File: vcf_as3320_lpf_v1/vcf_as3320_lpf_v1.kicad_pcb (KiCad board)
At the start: 2 copper layers, 15 x 100 mm, 87 parts, among them J1 Conn_02x05_Odd_Even, J4 IN1, J5 OUT_2, U1 LM358, U2 TL072, U3 AS3320, U4 LM79L05_TO92, U5 LM358

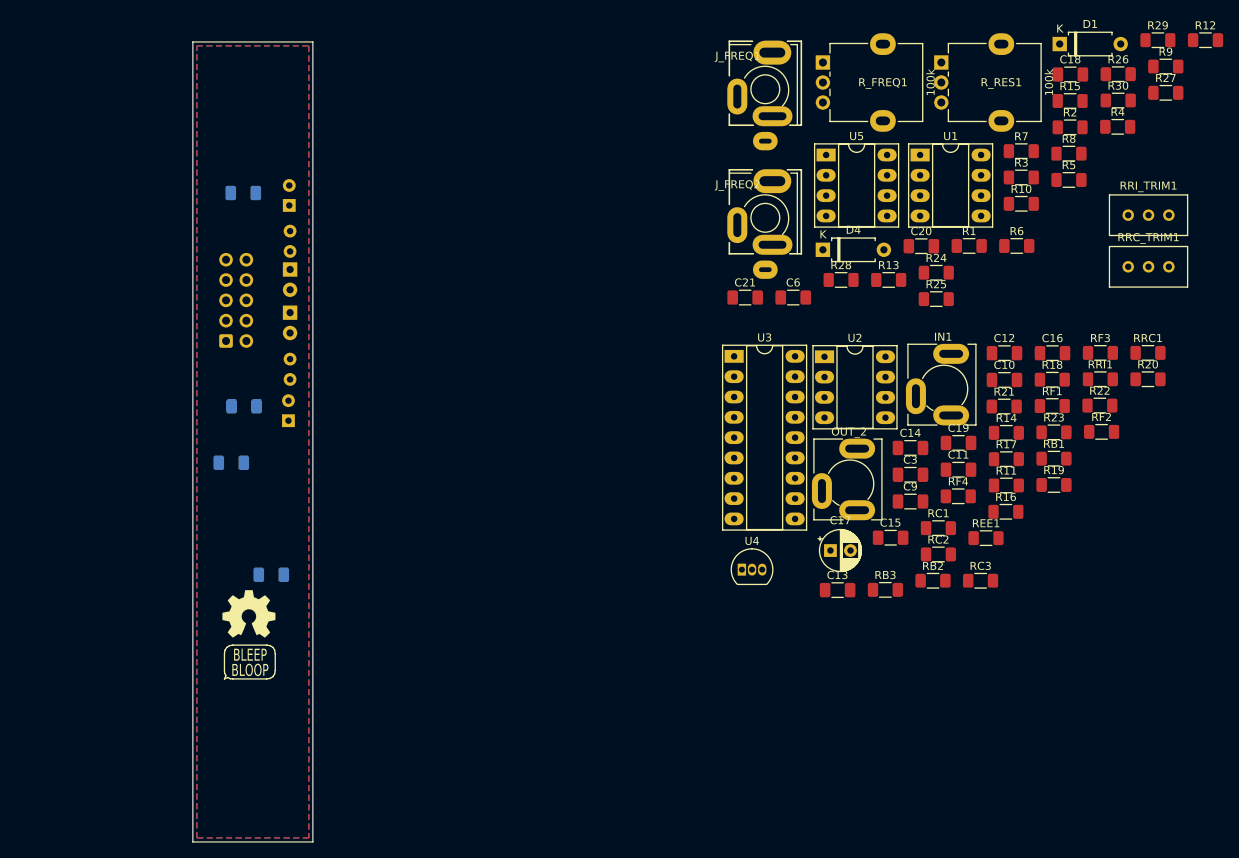
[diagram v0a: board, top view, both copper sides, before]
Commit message: Draft layout done no routing
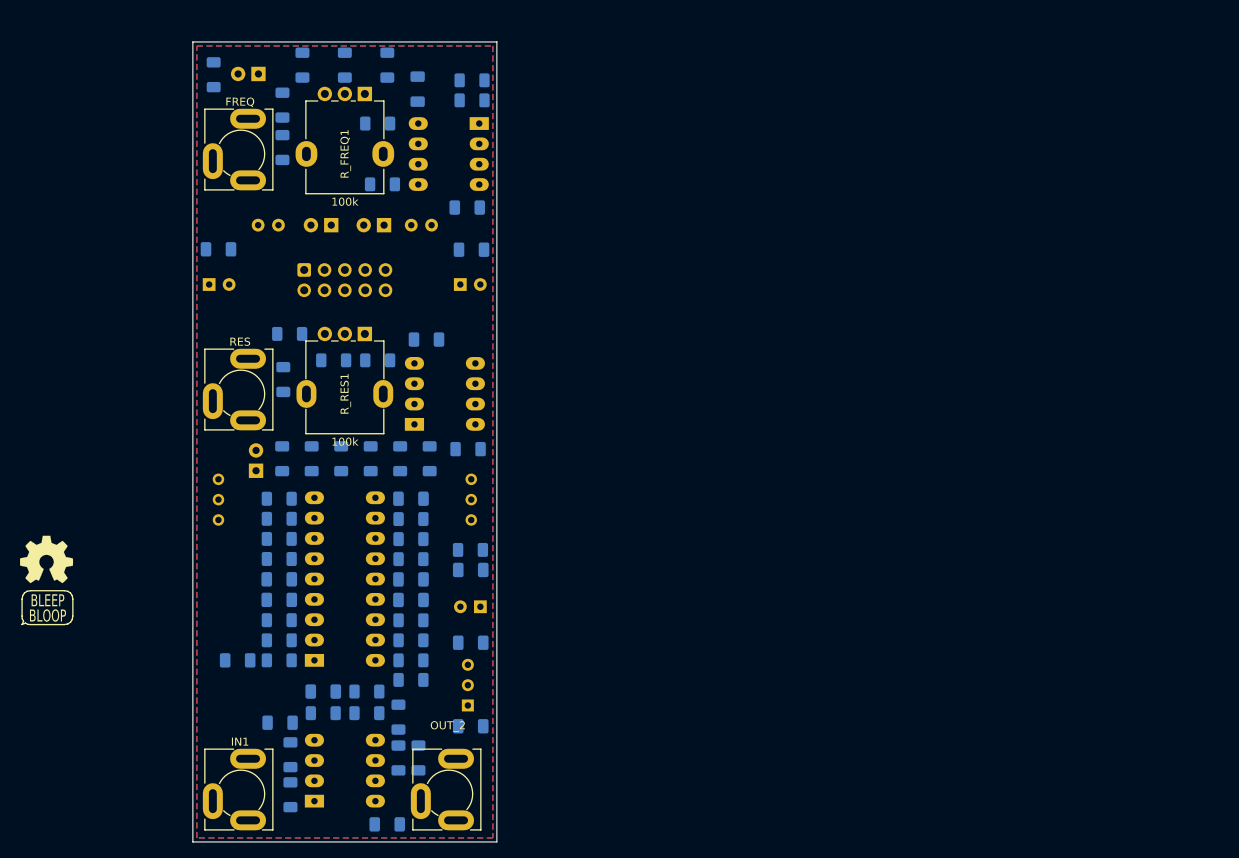
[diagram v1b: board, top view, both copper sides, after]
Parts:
- removed J_FREQ2: FREQ, My Stuff:Jack_3.5mm_MJ-355W_and_PJ398SM_Vertical
- added J_RES1: RES, My Stuff:Jack_3.5mm_MJ-355W_Vertical, F.Cu at (146.0, 94.0)
- C10, C11, C12, C13, C14, C15, C16, C17, C18, C19, C20, C21, C3, C6, C9, R1, R10, R11, R12, R13, R14, R15, R16, R17, R18, R19, R2, R20, R21, R22, R23, R24, R25, R26, R27, R28, R29, R3, R30, R4, R5, R6, R7, R8, R9, RB1, RB2, RB3, RC1, RC2, RC3, REE1, RF1, RF2, RF3, RF4, RRC1, RRC_TRIM1, RRI1, RRI_TRIM1, U1, U2, U3, U5: moved to B.Cu
- D1, D4: footprint Diode_THT:D_A-405_P7.62mm_Horizontal -> Diode_THT:D_A-405_P2.54mm_Vertical_KathodeUp; moved to B.Cu
- J_FREQ1: footprint My Stuff:Jack_3.5mm_MJ-355W_and_PJ398SM_Vertical -> My Stuff:Jack_3.5mm_MJ-355W_Vertical
- U4: footprint Package_TO_SOT_THT:TO-92_Inline -> Package_TO_SOT_THT:TO-92_Inline_Wide; moved to B.Cu
- moved RRI_TRIM1 124.8 mm to (143.2, 109.8), turned to -90 degrees
- moved R12 120.2 mm to (152.1, 86.5)
- moved R4 113.2 mm to (142.6, 54.1), turned to 90 degrees
- moved R30 110.3 mm to (154.9, 102.1), turned to -90 degrees
- moved R26 108.4 mm to (158.5, 102.1), turned to 90 degrees
- moved R27 106.1 mm to (165.9, 102.1), turned to 90 degrees
- moved RF3 105.8 mm to (150.8, 114.6)
- moved R29 105.0 mm to (169.6, 102.1), turned to 90 degrees
- moved RRI1 103.7 mm to (150.8, 107.1), turned to 180 degrees
- moved R22 103.6 mm to (150.8, 109.6)
- moved R20 102.8 mm to (165.7, 134.4), turned to 90 degrees
- moved J4 101.4 mm to (146.0, 144.0)
- moved D1 100.2 mm to (148.2, 54.0), turned to 180 degrees
- moved R9 99.0 mm to (163.7, 67.8)
- moved R2 98.5 mm to (151.2, 57.9), turned to -90 degrees
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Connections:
- R_FREQ1 pad 1: Net-(R2-Pad1) -> Net-(R1-Pad2)
- R_FREQ1 pad 3: Net-(R1-Pad2) -> Net-(R2-Pad1)
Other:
- board size 15 x 100 mm -> 38 x 100 mm
- board text added: "Make new fp for res pot for plastic trim pots"
- board text added: "feedback"
- board text added: "input"
- board text added: "output"

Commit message: Draft routing done
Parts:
- moved R12 13.9 mm to (166.0, 86.1), turned to 180 degrees
- moved R13 3.19 mm to (159.3, 92.5)
- moved LOGO3 2.84 mm to (121.2, 111.9)
- moved C21 2.31 mm to (171.4, 86.5)
- moved R7 0.70 mm to (174.2, 57.3)
- moved R8 0.70 mm to (174.2, 54.8)
- moved R15 0.70 mm to (162.4, 89.8)
- turned C20 to 180 degrees
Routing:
- net -12V: track 0.00 -> 188.2 mm, vias 0 -> 1
- net +12V: track 0.00 -> 157.1 mm, vias 0 -> 1
- net Net-(R17-Pad2): track 0.00 -> 67.2 mm
- net /CV Inputs/FREQ_CV: track 0.00 -> 63.4 mm, vias 0 -> 1
- net Net-(C3-Pad2): track 0.00 -> 30.9 mm
- net Net-(C19-Pad2): track 0.00 -> 30.2 mm
- net Net-(RC1-Pad2): track 0.00 -> 28.0 mm, vias 0 -> 1
- net Net-(RC2-Pad2): track 0.00 -> 26.5 mm, vias 0 -> 1
- net Net-(RRC1-Pad2): track 0.00 -> 25.5 mm
- net Net-(RC3-Pad2): track 0.00 -> 24.2 mm, vias 0 -> 1
- net Net-(R6-Pad1): track 0.00 -> 22.5 mm
- net Net-(J_FREQ1-PadT): track 0.00 -> 20.8 mm
- net /CV Inputs/RES_CV: track 0.00 -> 19.9 mm
- net Net-(R27-Pad1): track 0.00 -> 18.7 mm
- net -5V: track 0.00 -> 17.5 mm
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
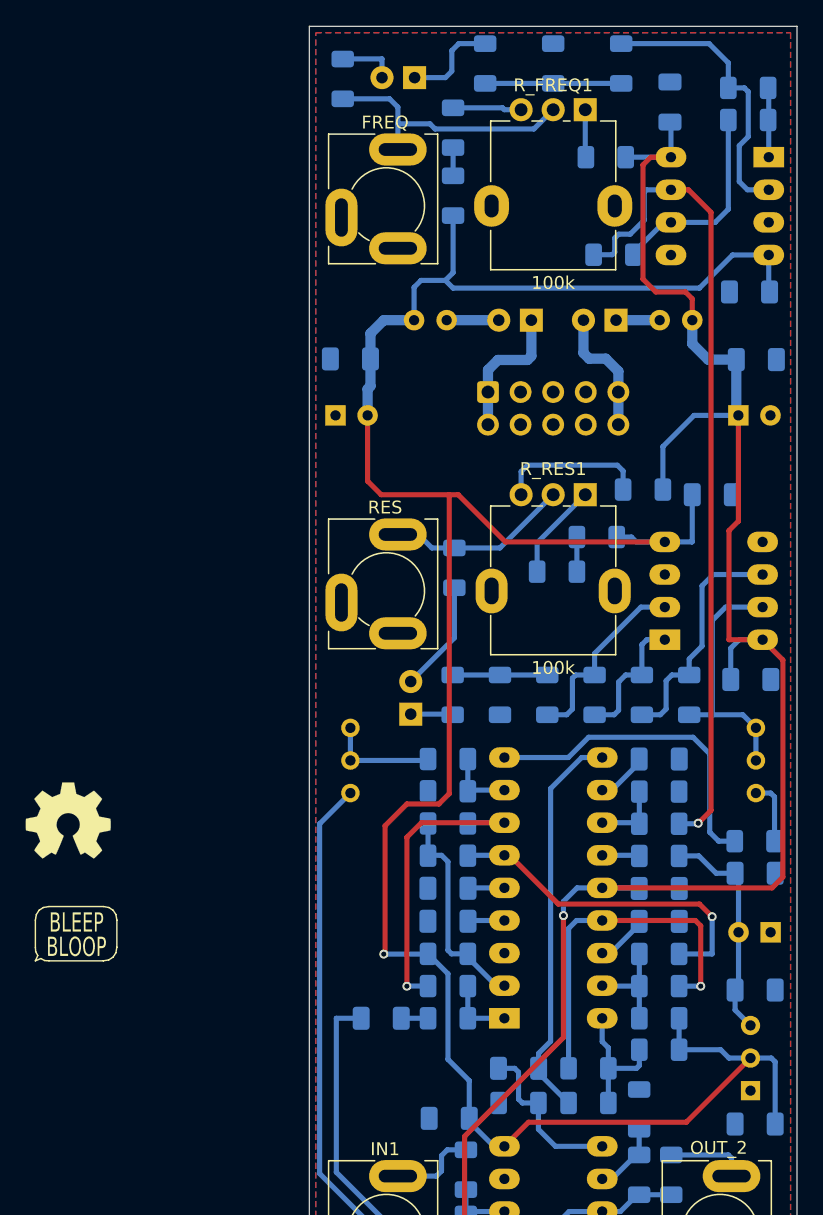
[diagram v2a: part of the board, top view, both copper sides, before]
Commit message: Geographic rename, silkscreen cleanup
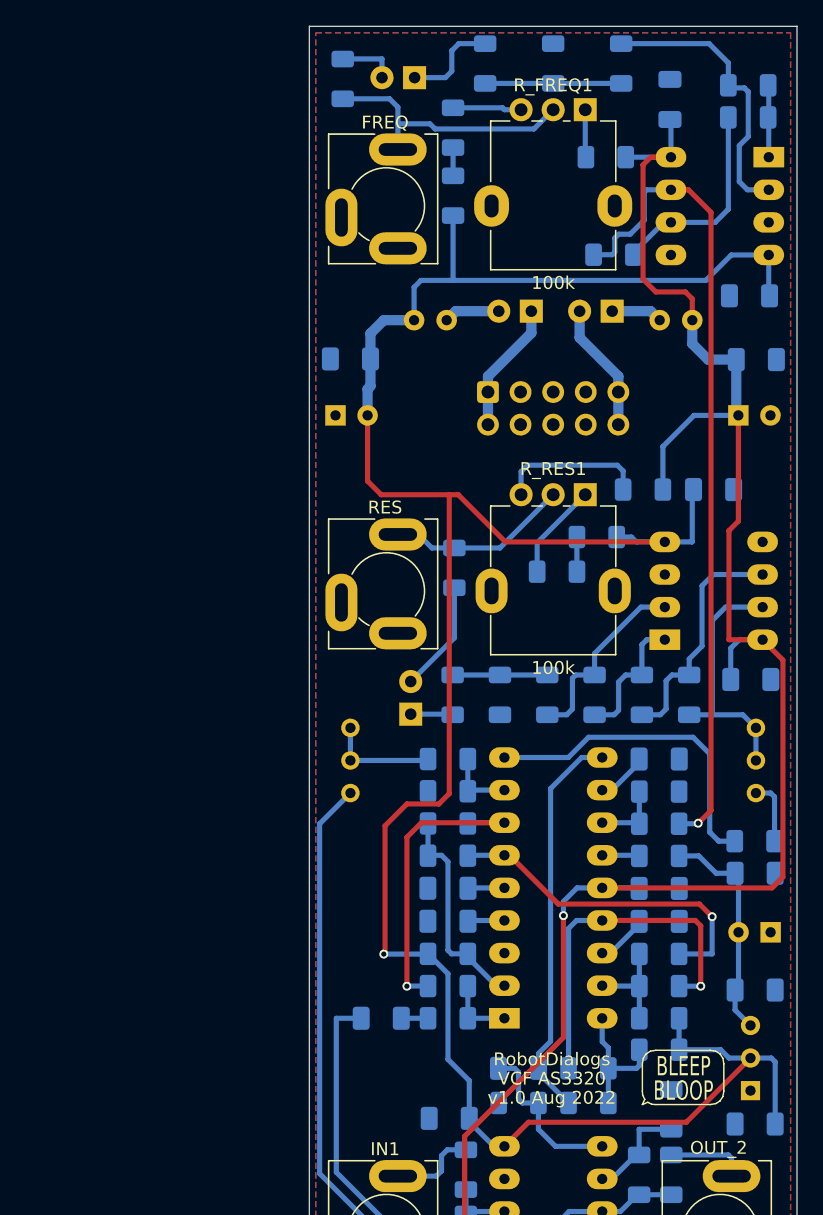
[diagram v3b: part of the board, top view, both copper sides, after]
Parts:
- D1, D2, D3, D4: value D -> 1N4001
- LOGO3: moved to B.Cu
- moved LOGO3 61.9 mm to (158.7, 62.6), turned to -45 degrees
- moved LOGO2 52.0 mm to (142.8, 121.8), turned to 90 degrees
- moved LOGO1 48.6 mm to (169.1, 131.9)
- moved R25 2.50 mm to (168.2, 134.4)
- moved D3 0.76 mm to (163.6, 72.2)
- moved D2 0.70 mm to (157.3, 72.2)
- moved C7 0.41 mm to (171.5, 86.1)
- moved C2 0.30 mm to (174.3, 71.0)
- moved C1 0.20 mm to (168.1, 55.7)
- moved R5 0.20 mm to (174.2, 54.6)
- moved R6 0.20 mm to (174.2, 57.1)
- renumbered C6 to C1, C14 to C10, C9 to C11, C10 to C12, C12 to C13, C11 to C14, C17 to C15, C19 to C17, C3 to C18, C8 to C19, C18 to C2, C15 to C20, C7 to C21, C4 to C3, C5 to C4, C1 to C5, C2 to C6, C21 to C7, C20 to C8, C13 to C9, R6 to R1, R9 to R10, R12 to R11, R15 to R12, R24 to R14, R29 to R15, R27 to R16, R28 to R17, R26 to R18, R30 to R19, R10 to R2, R25 to R20, R23 to R21, R21 to R23, R14 to R24, R20 to R25, R19 to R26, R17 to R27, R18 to R28, R11 to R29, R5 to R3, R16 to R30, R8 to R5, R7 to R6, R2 to R7, R1 to R8, R3 to R9, RB3 to RB1, RB1 to RB3, RC3 to RC2, RC2 to RC3, RC1 to RC4, RF4 to RF1, RF3 to RF2, RF2 to RF3, RF1 to RF4
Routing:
- net Net-(R28-Pad2): track 5.65 -> 8.15 mm
- net -12V: track 188.2 -> 187.4 mm
- net -12VA: track 10.9 -> 10.2 mm
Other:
- board text added: "AS3320"
- board text added: "FREQ CV"
- board text added: "IN"
- board text added: "LM358"
- board text added: "OUT"
- board text added: "RED"
- board text added: "RES CV"
- board text added: "TL072"
- board text added: "VCF AS3320"
- board text added: "v1.0 Aug 2022"
- board text removed: "Eurorack Template"
- board text removed: "Make new fp for res pot for plastic trim pots"
- board text removed: "feedback"
- board text removed: "input"
- board text removed: "output"
- board text removed: "v1.1 July 2022"
